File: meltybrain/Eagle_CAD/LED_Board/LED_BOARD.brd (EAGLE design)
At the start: 58.1 x 9.9 mm, 17 parts, among them J1 SM04B-SRSS-TB(LF)(SN)

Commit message: Update LED_BOARD.brd
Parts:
- moved C8 0.50 mm to (9.88, 1.52)
- moved C6 0.30 mm to (22.4, 1.52)
- moved C1 0.20 mm to (54.1, 1.58)
- moved C5 0.20 mm to (28.7, 1.52)
- moved C4 0.20 mm to (35.1, 1.53)
- moved C2 0.10 mm to (47.7, 1.53)
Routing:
- net GND: track 0.67 -> 31.3 mm, vias 0 -> 8
- net +5V: track 0.25 -> 29.8 mm, vias 0 -> 9

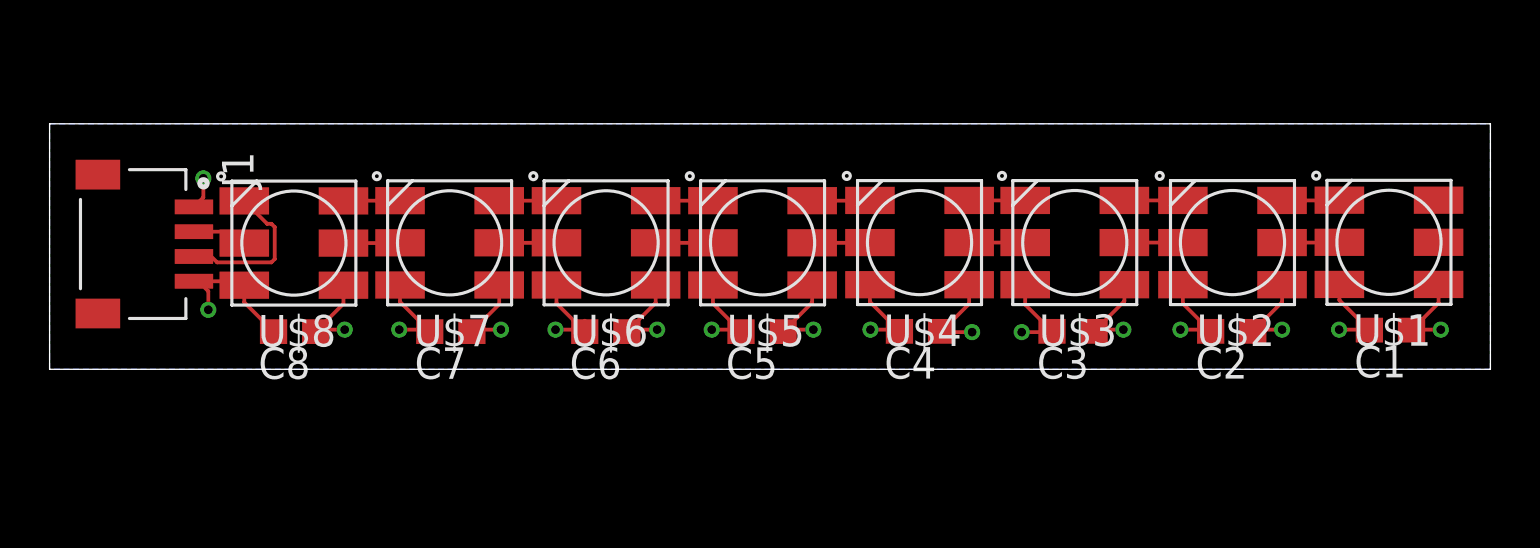
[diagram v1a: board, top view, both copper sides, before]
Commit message: Update LED_BOARD.brd
Added gornd and power planes
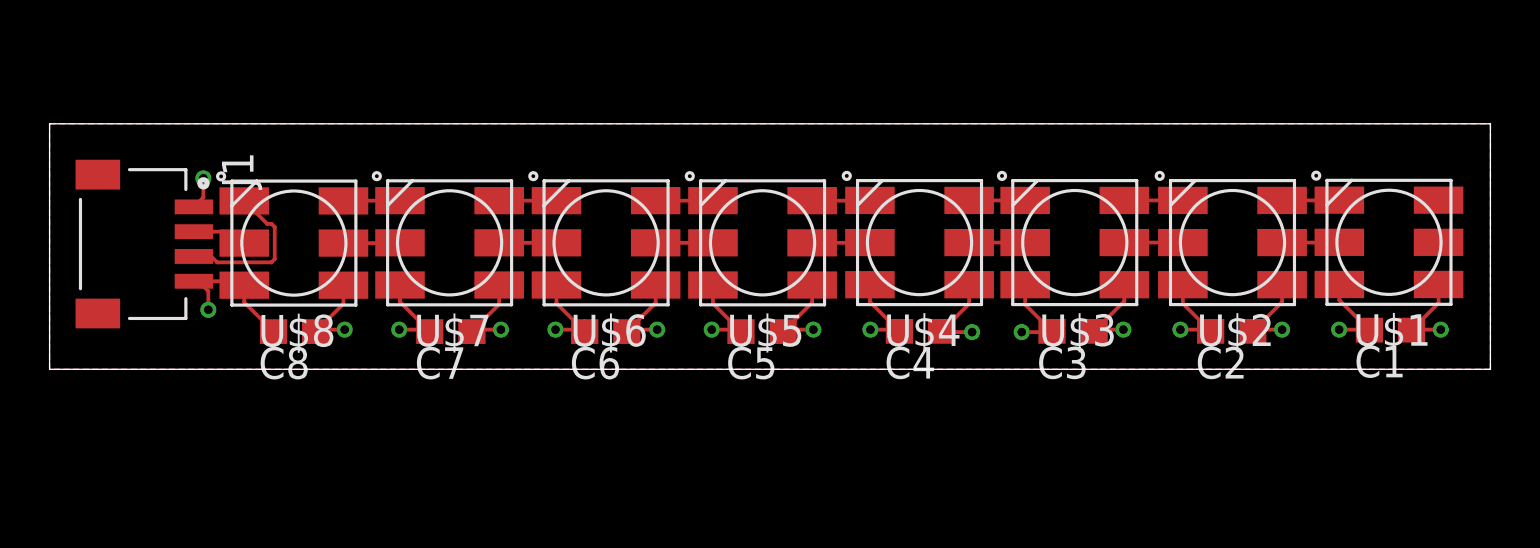
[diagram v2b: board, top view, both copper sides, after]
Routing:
- added copper zone on layer 1, net +5V
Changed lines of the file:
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@@
 <wire x1="56.1" y1="1.6" x2="54.94" y2="1.6" width="0.1524" layer="1"/>
 <wire x1="54.94" y1="1.6" x2="54.92" y2="1.58" width="0.1524" layer="1"/>
-<wire x1="49.7" y1="1.6" x2="54.92" y2="1.58" width="0" layer="19" extent="1-1"/>
-<wire x1="43.3" y1="1.6" x2="48.52" y2="1.53" width="0" layer="19" extent="1-1"/>
-<wire x1="37.2" y1="1.5" x2="42.12" y2="1.53" width="0" layer="19" extent="1-1"/>
-<wire x1="30.8" y1="1.6" x2="35.97" y2="1.53" width="0" layer="19" extent="1-1"/>
-<wire x1="24.5" y1="1.6" x2="29.58" y2="1.52" width="0" layer="19" extent="1-1"/>
-<wire x1="18.2" y1="1.6" x2="23.28" y2="1.52" width="0" layer="19" extent="1-1"/>
-<wire x1="11.9" y1="1.6" x2="17.03" y2="1.52" width="0" layer="19" extent="1-1"/>
-<wire x1="5.82" y1="6.55" x2="11.85" y2="3.39" width="0" layer="19" extent="1-1"/>
+<polygon width="0.1524" layer="1">
+<vertex x="0" y="0"/>
+<vertex x="0" y="9.9"/>
+<vertex x="58.1" y="9.9"/>
+<vertex x="58.1" y="0"/>
+</polygon>
 </signal>
 <signal name="GND">
@@
 <wire x1="6.4" y1="2.4" x2="6.4" y2="3.15" width="0.1524" layer="1"/>
 <wire x1="6.4" y1="3.15" x2="6" y2="3.55" width="0.1524" layer="1"/>
-<wire x1="46.82" y1="1.53" x2="52" y2="1.6" width="0" layer="19" extent="1-1"/>
-<wire x1="40.42" y1="1.53" x2="45.6" y2="1.6" width="0" layer="19" extent="1-1"/>
-<wire x1="34.27" y1="1.53" x2="39.2" y2="1.5" width="0" layer="19" extent="1-1"/>
-<wire x1="33.1" y1="1.6" x2="27.88" y2="1.52" width="0" layer="19" extent="1-1"/>
-<wire x1="21.58" y1="1.52" x2="26.7" y2="1.6" width="0" layer="19" extent="1-1"/>
-<wire x1="15.33" y1="1.52" x2="20.4" y2="1.6" width="0" layer="19" extent="1-1"/>
-<wire x1="9.03" y1="1.52" x2="14.1" y2="1.6" width="0" layer="19" extent="1-1"/>
 </signal>
 <signal name="N$15">

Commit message: Update LED_BOARD.brd
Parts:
- moved C3 0.10 mm to (41.4, 1.53)
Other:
- board size 58.1 x 9.9 mm -> 58 x 10 mm

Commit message: Update LED_BOARD.brd
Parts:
- moved C7 3.41 mm to (13.4, 3.50)
- moved C3 3.03 mm to (39.1, 3.53)
- moved C8 2.60 mm to (8.20, 3.50)
- moved C4 2.32 mm to (33.9, 3.50)
- moved C6 2.25 mm to (23.5, 3.50)
- moved U$1 2.13 mm to (53.0, 7.00)
- moved U$2 2.12 mm to (46.8, 7.00)
- moved C1 2.11 mm to (53.2, 3.50)
- moved U$3 2.07 mm to (40.5, 7.00)
- moved U$4 2.06 mm to (34.2, 7.00)
- moved U$5 2.04 mm to (28.0, 7.00)
- moved C5 2.03 mm to (28.7, 3.55)
- moved U$6 2.02 mm to (21.8, 7.00)
- moved U$8 2.00 mm to (9.25, 7.00)
- moved U$7 2.00 mm to (15.5, 7.00)
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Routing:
- net GND: track 31.4 -> 29.1 mm
- net +5V: track 29.8 -> 28.0 mm
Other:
- board size 58 x 10 mm -> 56.4 x 10 mm

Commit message: LED_BOARD update
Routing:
- net +5V: track 28.0 -> 1.40 mm, vias 9 -> 1
- net GND: track 29.1 -> 28.2 mm
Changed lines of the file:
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@@
 <attribute name="DKPN" value="455-1804-1-ND" x="-2.62" y="-25.35" size="1.778" layer="27" rot="R270" display="off"/>
 <attribute name="NAME" x="2.95381875" y="6.398059375" size="1.271490625" layer="25" rot="R180"/>
-<attribute name="VALUE" x="-7.756390625" y="6.505909375" size="1.27071875" layer="27" rot="R180"/>
+<attribute name="VALUE" x="3.194090625" y="7.843609375" size="0.4064" layer="27" rot="R270"/>
 </element>
 <element name="U$1" library="LED_BOARD" package="RGBLED5050" value="DOTSTAR" x="53" y="7" smashed="yes" rot="R180">
@@
 <contactref element="U$7" pad="1"/>
 <contactref element="U$8" pad="6"/>
-<wire x1="11.25" y1="8.7" x2="11.26" y2="8.8" width="0.1524" layer="1"/>
 <wire x1="11.25" y1="8.7" x2="13.5" y2="8.7" width="0.1524" layer="1"/>
 </signal>
@@
 <contactref element="J1" pad="1"/>
 <wire x1="17.5" y1="5.3" x2="17.063390625" y2="5.374003125" width="0.1524" layer="1"/>
-<wire x1="42.5" y1="5.3" x2="42.8" y2="5.41" width="0.1524" layer="1"/>
 <via x="5.15" y="8.8" extent="1-16" drill="0.35"/>
-<via x="10.2" y="3.5" extent="1-16" drill="0.35"/>
-<via x="15.4" y="3.5" extent="1-16" drill="0.35"/>
-<via x="25.5" y="3.5" extent="1-16" drill="0.35"/>
-<via x="30.7" y="3.5" extent="1-16" drill="0.35"/>
-<via x="35.9" y="3.5" extent="1-16" drill="0.35"/>
-<via x="50" y="3.5" extent="1-16" drill="0.35"/>
-<via x="55.2" y="3.5" extent="1-16" drill="0.35"/>
-<via x="41.1" y="3.5" extent="1-16" drill="0.35"/>
 <polygon width="0.1524" layer="1">
 <vertex x="0" y="0"/>
@@
 <wire x1="5" y1="7.9" x2="5.15" y2="8.05" width="0.1524" layer="1"/>
 <wire x1="5.15" y1="8.05" x2="5.15" y2="8.8" width="0.1524" layer="1"/>
-<wire x1="9.05" y1="3.5" x2="10.2" y2="3.5" width="0.1524" layer="1"/>
-<wire x1="10.2" y1="3.5" x2="11.25" y2="4.55" width="0.1524" layer="1"/>
-<wire x1="11.25" y1="4.55" x2="11.25" y2="5.3" width="0.1524" layer="1"/>
-<wire x1="17.063390625" y1="5.163390625" x2="17.063390625" y2="5.374003125" width="0.1524" layer="1"/>
-<wire x1="29.6" y1="3.5" x2="29.55" y2="3.55" width="0.1524" layer="1"/>
-<wire x1="35.9" y1="4.9" x2="36" y2="5" width="0.1524" layer="1"/>
-<wire x1="39.98" y1="3.5" x2="39.95" y2="3.53" width="0.1524" layer="1"/>
-<wire x1="14.25" y1="3.5" x2="15.4" y2="3.5" width="0.1524" layer="1"/>
-<wire x1="15.4" y1="3.5" x2="17.063390625" y2="5.163390625" width="0.1524" layer="1"/>
-<wire x1="24.35" y1="3.5" x2="23.75" y2="4.1" width="0.1524" layer="1"/>
-<wire x1="23.75" y1="4.1" x2="23.75" y2="5.3" width="0.1524" layer="1"/>
-<wire x1="24.35" y1="3.5" x2="25.5" y2="3.5" width="0.1524" layer="1"/>
-<wire x1="29.55" y1="3.55" x2="29.55" y2="4.85" width="0.1524" layer="1"/>
-<wire x1="29.55" y1="4.85" x2="30" y2="5.3" width="0.1524" layer="1"/>
-<wire x1="30.7" y1="3.5" x2="29.6" y2="3.5" width="0.1524" layer="1"/>
-<wire x1="34.75" y1="3.5" x2="35.9" y2="3.5" width="0.1524" layer="1"/>
-<wire x1="35.9" y1="3.5" x2="35.9" y2="4.95" width="0.1524" layer="1"/>
-<wire x1="35.9" y1="4.95" x2="36.25" y2="5.3" width="0.1524" layer="1"/>
-<wire x1="39.95" y1="3.53" x2="41.07" y2="3.53" width="0.1524" layer="1"/>
-<wire x1="41.07" y1="3.53" x2="41.1" y2="3.5" width="0.1524" layer="1"/>
-<wire x1="41.1" y1="3.5" x2="42.5" y2="4.9" width="0.1524" layer="1"/>
-<wire x1="42.5" y1="4.9" x2="42.5" y2="5.3" width="0.1524" layer="1"/>
-<wire x1="55.2" y1="3.5" x2="55.2" y2="5.1" width="0.1524" layer="1"/>
-<wire x1="55.2" y1="5.1" x2="55" y2="5.3" width="0.1524" layer="1"/>
-<wire x1="54.05" y1="3.5" x2="55.2" y2="3.5" width="0.1524" layer="1"/>
-<wire x1="50" y1="3.5" x2="48.85" y2="3.5" width="0.1524" layer="1"/>
-<wire x1="48.85" y1="3.5" x2="48.85" y2="5.2" width="0.1524" layer="1"/>
-<wire x1="48.85" y1="5.2" x2="48.75" y2="5.3" width="0.1524" layer="1"/>
-<wire x1="36.25" y1="5.3" x2="36" y2="5" width="0" layer="19" extent="1-1"/>
 </signal>
 <signal name="GND">
@@
 <vertex x="0" y="10"/>
 </polygon>
-<wire x1="7.09" y1="5.55" x2="7.25" y2="5.3" width="0.1524" layer="1"/>
 <via x="5.2" y="4" extent="1-16" drill="0.35"/>
 <via x="11.4" y="3.5" extent="1-16" drill="0.35"/>
@@
 <via x="46" y="3.5" extent="1-16" drill="0.35"/>
 <via x="51.2" y="3.5" extent="1-16" drill="0.35"/>
-<wire x1="23" y1="3.6" x2="22.65" y2="3.5" width="0.1524" layer="1"/>
 <wire x1="5.2" y1="4.7" x2="5.2" y2="4" width="0.1524" layer="1"/>
 <wire x1="5.2" y1="4.7" x2="5" y2="4.9" width="0.1524" layer="1"/>
-<wire x1="5" y1="4.9" x2="5.1" y2="5" width="0.1524" layer="1"/>
 <wire x1="22.65" y1="3.5" x2="21.5" y2="3.5" width="0.1524" layer="1"/>
 <wire x1="21.5" y1="3.5" x2="19.75" y2="5.25" width="0.1524" layer="1"/>
 <wire x1="19.75" y1="5.25" x2="19.75" y2="5.3" width="0.1524" layer="1"/>
 <wire x1="27.8" y1="3.5" x2="27.85" y2="3.55" width="0.1524" layer="1"/>
-<wire x1="26.7" y1="5.2" x2="26.75" y2="5.25" width="0.1524" layer="1"/>
-<wire x1="38.22" y1="3.5" x2="38.25" y2="3.53" width="0.1524" layer="1"/>
 <wire x1="5" y1="4.9" x2="6.85" y2="4.9" width="0.1524" layer="1"/>
 <wire x1="6.85" y1="4.9" x2="7.25" y2="5.3" width="0.1524" layer="1"/>
@@
 <wire x1="12.55" y1="3.5" x2="13.5" y2="4.45" width="0.1524" layer="1"/>
 <wire x1="13.5" y1="4.45" x2="13.5" y2="5.3" width="0.1524" layer="1"/>
-<wire x1="26" y1="5.3" x2="26.7" y2="4.6" width="0.1524" layer="1"/>
-<wire x1="26.7" y1="4.6" x2="26.7" y2="3.5" width="0.1524" layer="1"/>
 <wire x1="26.7" y1="3.5" x2="27.8" y2="3.5" width="0.1524" layer="1"/>
 <wire x1="32.25" y1="5.3" x2="31.9" y2="4.95" width="0.1524" layer="1"/>
@@
 <wire x1="46" y1="3.5" x2="44.75" y2="4.75" width="0.1524" layer="1"/>
 <wire x1="44.75" y1="4.75" x2="44.75" y2="5.3" width="0.1524" layer="1"/>
-<wire x1="26" y1="5.3" x2="26.7" y2="5.2" width="0" layer="19" extent="1-1"/>
+<wire x1="26.7" y1="3.5" x2="26" y2="4.2" width="0.1524" layer="1"/>
+<wire x1="26" y1="4.2" x2="26" y2="5.3" width="0.1524" layer="1"/>
 </signal>
 <signal name="N$15">
 <contactref element="U$8" pad="2"/>
 <contactref element="J1" pad="2"/>
-<wire x1="5" y1="6.9" x2="5.16" y2="6.99" width="0.1524" layer="1"/>
 <wire x1="7.25" y1="7" x2="7.01" y2="6.85" width="0.1524" layer="1"/>
 <wire x1="7.01" y1="6.85" x2="5" y2="6.9" width="0.1524" layer="1"/>

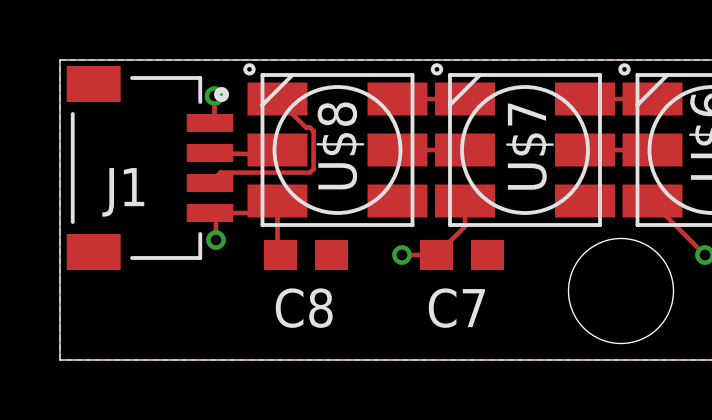
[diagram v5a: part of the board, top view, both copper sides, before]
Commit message: Edited silkscreen and made minor changes to IR Receiver silkscreen and schematic
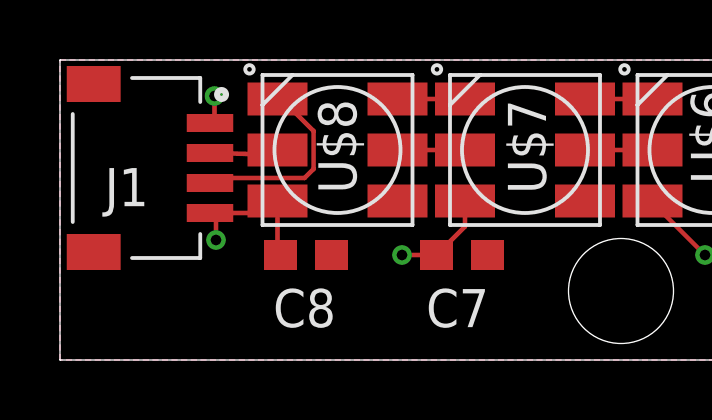
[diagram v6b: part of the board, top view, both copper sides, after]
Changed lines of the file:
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@@
 <?xml version="1.0" encoding="utf-8"?>
 <!DOCTYPE eagle SYSTEM "eagle.dtd">
-<eagle version="9.5.1">
+<eagle version="9.6.2">
 <drawing>
 <settings>
-<setting alwaysvectorfont="no"/>
+<setting alwaysvectorfont="yes"/>
 <setting verticaltext="up"/>
 </settings>
-<grid distance="1" unitdist="mm" unit="mm" style="lines" multiple="1" display="no" altdistance="0.1" altunitdist="mm" altunit="mm"/>
+<grid distance="1" unitdist="mm" unit="mm" style="lines" multiple="1" display="no" altdistance="0.01" altunitdist="mm" altunit="mm"/>
 <layers>
 <layer number="1" name="Top" color="4" fill="1" visible="yes" active="yes"/>
@@
 <contactref element="U$8" pad="1"/>
 <contactref element="J1" pad="3"/>
-<wire x1="8.33416875" y1="6.2468" x2="8.4532" y2="6.36583125" width="0.1524" layer="1"/>
+<wire x1="8.15416875" y1="6.0668" x2="8.4532" y2="6.36583125" width="0.1524" layer="1"/>
 <wire x1="8.4532" y1="6.36583125" x2="8.4532" y2="7.63416875" width="0.1524" layer="1"/>
-<wire x1="8.4532" y1="7.63416875" x2="8.33416875" y2="7.7532" width="0.1524" layer="1"/>
-<wire x1="8.33416875" y1="7.7532" x2="8.1968" y2="7.7532" width="0.1524" layer="1"/>
-<wire x1="8.1968" y1="7.7532" x2="7.25" y2="8.7" width="0.1524" layer="1"/>
-<wire x1="5" y1="5.9" x2="5.3468" y2="6.2468" width="0.1524" layer="1"/>
-<wire x1="5.3468" y1="6.2468" x2="8.33416875" y2="6.2468" width="0.1524" layer="1"/>
+<wire x1="8.4532" y1="7.63416875" x2="7.46416875" y2="8.6232" width="0.1524" layer="1"/>
+<wire x1="7.46416875" y1="8.6232" x2="7.25" y2="8.6232" width="0.1524" layer="1"/>
+<wire x1="7.25" y1="8.6232" x2="7.25" y2="8.7" width="0.1524" layer="1"/>
+<wire x1="5" y1="5.9" x2="5.1668" y2="6.0668" width="0.1524" layer="1"/>
+<wire x1="5.1668" y1="6.0668" x2="8.15416875" y2="6.0668" width="0.1524" layer="1"/>
 </signal>
 </signals>

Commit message: Edited LED board to add 3d packages.  Made cosmetic changes to Control in preparation for design review
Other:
- outline, holes or cut-outs redrawn
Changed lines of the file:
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@@
 <drawing>
 <settings>
-<setting alwaysvectorfont="yes"/>
+<setting alwaysvectorfont="no"/>
 <setting verticaltext="up"/>
 </settings>
@@
 </layers>
 <board>
+<fusionsync huburn="a.cGVyc29uYWw6dWUyY2EyMWFk" projecturn="a.cGVyc29uYWw6dWUyZDhlY2M3IzIwMjAwNzEyMzE1MDc1MjU2" f3durn="urn:adsk.wipprod:dm.lineage:YHiRqw0lT8mW9qK3G1eB8g" pcbguid="" lastpulledtime="2020-08-20T22:57:00Z" lastsyncedchangeguid="" latestrevisionid="a908691b-5d7b-4b37-ad4e-dc1c596d2ba9" lastsyncedrevisionid="7882eff3-3246-4c77-b9dc-e37fc00316f1" lastboardhashguid="77dea297-f60c-e6e3-4bac-979240e8aa8b" lastpushedtime="2020-08-20T22:48:46Z" linktopcb3d="true"/>
 <plain>
+<dimension x1="0" y1="10" x2="56.4" y2="10" x3="28.2" y3="13" textsize="1.778" layer="1"/>
+<dimension x1="0" y1="0" x2="0" y2="10" x3="-2" y3="5" textsize="1.778" layer="1"/>
+<circle x="43.7" y="2.5" radius="1.75" width="0" layer="20"/>
+<circle x="18.7" y="2.3" radius="1.75" width="0" layer="20"/>
+<wire x1="0" y1="10" x2="0" y2="0" width="0" layer="20"/>
 <wire x1="0" y1="0" x2="56.4" y2="0" width="0" layer="20"/>
 <wire x1="56.4" y1="0" x2="56.4" y2="10" width="0" layer="20"/>
-<wire x1="0" y1="10" x2="56.4" y2="10" width="0" layer="20"/>
-<wire x1="0" y1="0" x2="0" y2="10" width="0" layer="20"/>
-<hole x="18.7" y="2.3" drill="3.5"/>
-<hole x="43.7" y="2.5" drill="3.5"/>
-<dimension x1="0" y1="10" x2="56.4" y2="10" x3="28.2" y3="13" textsize="1.778" layer="1"/>
-<dimension x1="0" y1="0" x2="0" y2="10" x3="-2" y3="5" textsize="1.778" layer="1"/>
+<wire x1="56.4" y1="10" x2="0" y2="10" width="0" layer="20"/>
 </plain>
 <attributes>
@@
 <attribute name="VALUE" x="3.194090625" y="7.843609375" size="0.4064" layer="27" rot="R270"/>
 </element>
-<element name="U$1" library="LED_BOARD" package="RGBLED5050" value="DOTSTAR" x="53" y="7" smashed="yes" rot="R180">
+<element name="U$1" library="LED_BOARD" package="RGBLED5050" package3d_urn="urn:adsk.eagle:package:22765567/2" value="DOTSTAR" x="53" y="7" smashed="yes" rot="R180">
 <attribute name="NAME" x="53.54" y="5.88" size="1.27" layer="25" font="vector" rot="R90"/>
 </element>
-<element name="U$2" library="LED_BOARD" package="RGBLED5050" value="DOTSTAR" x="46.75" y="7" smashed="yes" rot="R180">
+<element name="U$2" library="LED_BOARD" package="RGBLED5050" package3d_urn="urn:adsk.eagle:package:22765567/2" value="DOTSTAR" x="46.75" y="7" smashed="yes" rot="R180">
 <attribute name="NAME" x="47.42" y="5.65" size="1.27" layer="25" font="vector" rot="R90"/>
 </element>
-<element name="U$3" library="LED_BOARD" package="RGBLED5050" value="DOTSTAR" x="40.5" y="7" smashed="yes" rot="R180">
+<element name="U$3" library="LED_BOARD" package="RGBLED5050" package3d_urn="urn:adsk.eagle:package:22765567/2" value="DOTSTAR" x="40.5" y="7" smashed="yes" rot="R180">
 <attribute name="NAME" x="41.22" y="5.72" size="1.27" layer="25" font="vector" rot="R90"/>
 </element>
-<element name="U$4" library="LED_BOARD" package="RGBLED5050" value="DOTSTAR" x="34.25" y="7" smashed="yes" rot="R180">
+<element name="U$4" library="LED_BOARD" package="RGBLED5050" package3d_urn="urn:adsk.eagle:package:22765567/2" value="DOTSTAR" x="34.25" y="7" smashed="yes" rot="R180">
 <attribute name="NAME" x="34.82" y="5.79" size="1.27" layer="25" font="vector" rot="R90"/>
 </element>
-<element name="U$5" library="LED_BOARD" package="RGBLED5050" value="DOTSTAR" x="28" y="7" smashed="yes" rot="R180">
+<element name="U$5" library="LED_BOARD" package="RGBLED5050" package3d_urn="urn:adsk.eagle:package:22765567/2" value="DOTSTAR" x="28" y="7" smashed="yes" rot="R180">
 <attribute name="NAME" x="28.7" y="5.8" size="1.27" layer="25" font="vector" rot="R90"/>
 </element>
-<element name="U$6" library="LED_BOARD" package="RGBLED5050" value="DOTSTAR" x="21.75" y="7" smashed="yes" rot="R180">
+<element name="U$6" library="LED_BOARD" package="RGBLED5050" package3d_urn="urn:adsk.eagle:package:22765567/2" value="DOTSTAR" x="21.75" y="7" smashed="yes" rot="R180">
 <attribute name="NAME" x="22.3" y="5.87" size="1.27" layer="25" font="vector" rot="R90"/>
 </element>
-<element name="U$7" library="LED_BOARD" package="RGBLED5050" value="DOTSTAR" x="15.5" y="7" smashed="yes" rot="R180">
+<element name="U$7" library="LED_BOARD" package="RGBLED5050" package3d_urn="urn:adsk.eagle:package:22765567/2" value="DOTSTAR" x="15.5" y="7" smashed="yes" rot="R180">
 <attribute name="NAME" x="16.2" y="5.54" size="1.27" layer="25" font="vector" rot="R90"/>
 </element>
-<element name="U$8" library="LED_BOARD" package="RGBLED5050" value="DOTSTAR" x="9.25" y="7" smashed="yes" rot="R180">
+<element name="U$8" library="LED_BOARD" package="RGBLED5050" package3d_urn="urn:adsk.eagle:package:22765567/2" value="DOTSTAR" x="9.25" y="7" smashed="yes" rot="R180">
 <attribute name="NAME" x="9.88" y="5.55" size="1.27" layer="25" font="vector" rot="R90"/>
 </element>
@@
 </note>
 <note version="8.3" severity="warning">
+Since Version 8.3, EAGLE supports Fusion synchronisation.
+This feature will not be available in this version and saving
+the document will break the link to the Fusion PCB feature.
+</note>
+<note version="8.3" severity="warning">
